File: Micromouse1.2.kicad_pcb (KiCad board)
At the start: 2 copper layers, 70.4 x 87.9 mm, 117 parts, among them J1 USB_B, P1 CONN_01X4, Q1 Q_NMOS_DGS, Q2 Q_NMOS_DGS, Q3 Q_NMOS_DGS, Q4 Q_NMOS_DGS, Q5 Q_NMOS_DGS, Q6 Q_NMOS_DGS, U1 BAT54C, U10 CONN_02X03, U14 ferrite, U15 LMZ21701, U16 JST_Connector, U17 Switch_micromouse, U18 LMZ21701, U19 splitter, U2 DRV8833, U20 TPD3S014, U21 MKL02Z32VFG4, U22 LP38691, U23 MK66FX1M0, U24 Test_Point, U25 Test_Point, U26 Test_Point, U27 Test_Point, U28 Test_Point, U29 Test_Point, U3 ferrite, U30 Test_Point, U31 MPU-6500, U32 Motor_mount, U5 ferrite, U6 BAT54C, U9 CONN_02X03, Y1 Crystal_16MHz, Y2 32.768MHz

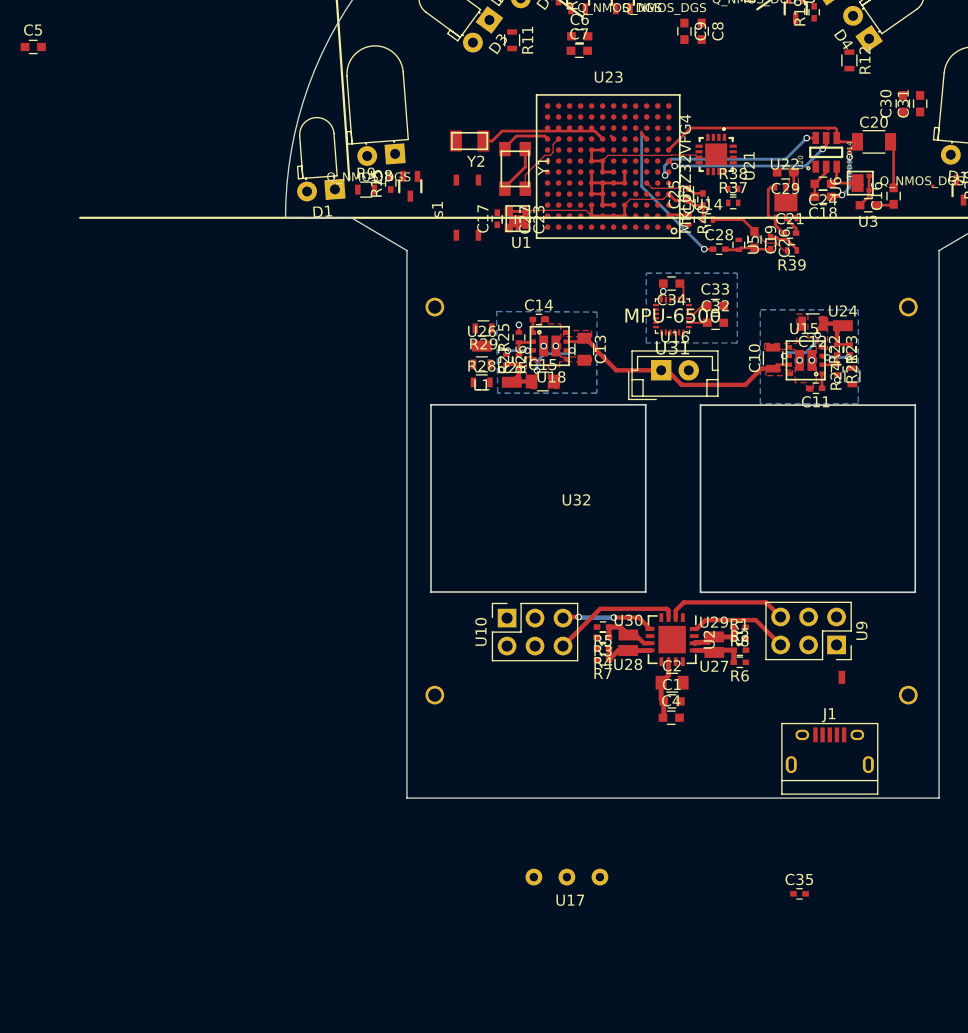
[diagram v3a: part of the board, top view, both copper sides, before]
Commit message: changed the MCU to MK20DX256VLH7
-changed the MCU to MK20DX256VLH7
-This branch is deprciated as I am changing back to the K66 series MCU
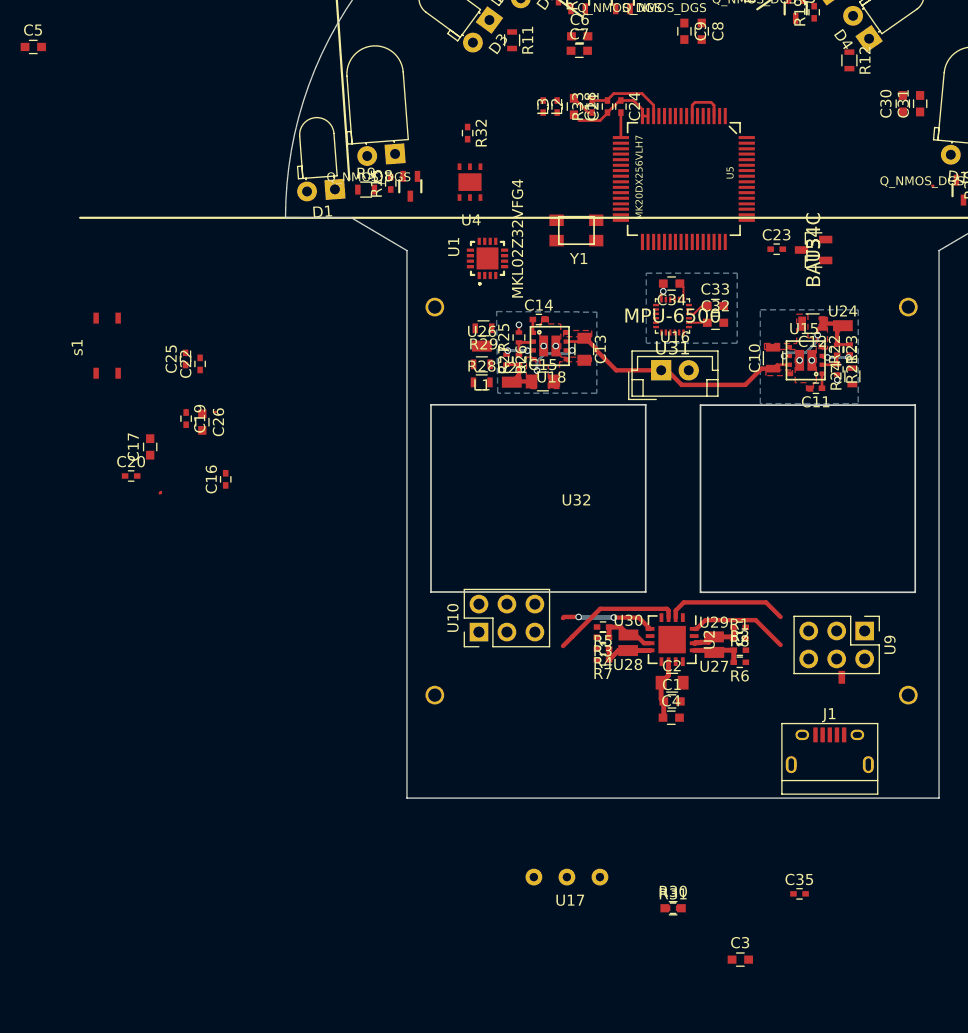
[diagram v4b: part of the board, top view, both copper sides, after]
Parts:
- removed C27, C29: 2.2uF, micromouse:C_0603
- removed C28: 0.1uF, micromouse:C_0402
- removed R37, R38: 33, Resistors_SMD:R_0402
- removed R39: 470, micromouse:R_0402
- removed R40: 100k, micromouse:R_0402
- removed U14: ferrite, micromouse:R_0402
- removed U20: TPD3S014, micromouse:TPD3S014
- removed U21: MKL02Z32VFG4, micromouse:MKL02Z32VFG4
- removed U22: LP38691, micromouse:LP38691
- removed U23: MK66FX1M0, micromouse:Microcontroller
- removed U6: BAT54C, micromouse:PMEG4010_DIODE
- removed Y2: 32.768MHz, micromouse:32.768_CRYSTAL
- added C3: 0.01uF, Capacitors_SMD:C_0603, F.Cu at (124.9, 129.1)
- added L2: Ferrite_Bead_Small, micromouse:C_0402, F.Cu at (107.0, 51.7)
- added L3: Ferrite_Bead_Small, micromouse:C_0402, F.Cu at (108.2, 51.7)
- added R30: R, micromouse:C_0603, F.Cu at (118.8, 124.5)
- added R31: 33, micromouse:C_0402, F.Cu at (118.8, 124.5)
- added R32: 33, micromouse:C_0402, F.Cu at (100.1, 54.1)
- added R33: 470, micromouse:C_0402, F.Cu at (111.4, 51.7)
- added U4: LP38691, micromouse:LP38691, F.Cu at (100.4, 58.5)
- C16: footprint micromouse:C_0603 -> Capacitors_SMD:C_0402
- C17, C26: value 0.1uF -> 2.2uF; footprint micromouse:C_0402 -> micromouse:C_0603
- C19, C24: value 2.2uF -> 0.1uF; footprint micromouse:C_0603 -> Capacitors_SMD:C_0402
- C20: value 100uF -> 0.1uF; footprint micromouse:C_1206 -> Capacitors_SMD:C_0402
- C21, C22: footprint micromouse:C_0402 -> Capacitors_SMD:C_0402
- C23: value 10nF -> 0.1uF; footprint micromouse:C_0402 -> Capacitors_SMD:C_0402
- C25: value 10nF -> 2.2uF; footprint micromouse:C_0402 -> Capacitors_SMD:C_0402
- J1: value USB_B -> USB_OTG
- U1: value BAT54C -> MKL02Z32VFG4; footprint micromouse:PMEG4010_DIODE -> micromouse:MKL02Z32VFG4
- U10, U9: footprint micromouse:Motors_connectors -> micromouse:Motor_Connector
- U3: value ferrite -> BAT54C; footprint micromouse:C_0603 -> PJC-Sandbox:SOT23-3P95_240X120L20X48N
- U5: value ferrite -> MK20DX256VLH7; footprint micromouse:R_0402 -> micromouse:LQFP-64
- Y1: value Crystal_16MHz -> Crystal_GND2
- moved C20 74.0 mm to (69.5, 85.2)
- moved C16 65.9 mm to (78.1, 85.5)
- moved C19 54.1 mm to (74.5, 80.0)
- moved C26 54.1 mm to (76.0, 80.3)
- moved C22 48.0 mm to (75.8, 75.0)
- moved C25 48.0 mm to (74.5, 74.6)
- moved C17 37.7 mm to (71.3, 82.6)
- moved s1 35.0 mm to (67.4, 73.4)
- moved C18 24.1 mm to (109.8, 51.7), turned to 270 degrees
- moved C23 23.0 mm to (128.2, 64.6), turned to 0 degrees
- moved C21 20.2 mm to (112.8, 51.7), turned to 90 degrees
- moved C24 19.6 mm to (114.0, 51.7), turned to 270 degrees
- moved Y1 7.89 mm to (110.0, 62.9), turned to 0 degrees
- moved U5 7.79 mm to (119.7, 58.2)
- moved U3 6.42 mm to (131.5, 64.7), turned to 90 degrees
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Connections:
- C17 pad 1: Net-(C17-Pad1) -> V_BAT
- C18 pad 2: GNDD -> Net-(C18-Pad2)
- C19 pad 2: Net-(C19-Pad2) -> GNDD
- C20 pad 1: Net-(C18-Pad1) -> Net-(C19-Pad1)
- C21 pad 1: Net-(C21-Pad1) -> Net-(C18-Pad2)
- C21 pad 2: GNDD -> Net-(C21-Pad2)
- C22 pad 1: Net-(C22-Pad1) -> Net-(C19-Pad1)
- C23 pad 1: Net-(C22-Pad1) -> Net-(C23-Pad1)
- C24 pad 1: Net-(C21-Pad1) -> Net-(C18-Pad2)
- C24 pad 2: GNDD -> Net-(C24-Pad2)
- C25 pad 1: Net-(C22-Pad1) -> Net-(C19-Pad1)
- C26 pad 1: Net-(C26-Pad1) -> Net-(C19-Pad1)
- C26 pad 2: Net-(C19-Pad2) -> GNDD
- J1 pad 1: Net-(J1-Pad1) -> Net-(C16-Pad1)
- J1 pad 5: Net-(J1-Pad5) -> GNDD
- J1 pad 6: (no net) -> GNDD
- U1 pad 1: Net-(C22-Pad1) -> Net-(C19-Pad1)
- U1 pad 2: Net-(U1-Pad2) -> GNDD
- U1 pad 3: Net-(C17-Pad1) -> Net-(U1-Pad3)
- U3 pad 1: Net-(C16-Pad1) -> Net-(C19-Pad1)
- U3 pad 2: Net-(U3-Pad2) -> V_BAT
- U5 pad 1: GNDD -> Net-(U5-Pad1)
- U5 pad 2: Net-(C19-Pad2) -> Net-(U5-Pad2)
- Y1 pad 1: Net-(U23-PadM12) -> Net-(U5-Pad32)
- Y1 pad 3: Net-(U23-PadM11) -> Net-(U5-Pad33)
- s1 pad 1: Net-(U21-Pad10) -> Net-(U1-Pad10)
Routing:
- net Net-(C22-Pad1): track 34.6 -> 0.00 mm, vias 1 -> 0
- net GNDD: track 35.2 -> 2.73 mm
- net Net-(R37-Pad1): track 16.0 -> 0.00 mm
- net Net-(U20-Pad6): track 15.8 -> 0.00 mm, vias 2 -> 0
- net Net-(C28-Pad1): track 13.8 -> 0.00 mm, vias 1 -> 0
- net Net-(U23-PadM7): track 11.5 -> 0.00 mm
- net Net-(C21-Pad1): track 10.3 -> 0.00 mm
- net Net-(C18-Pad2): track 0.00 -> 8.67 mm
- net Net-(C21-Pad2): track 0.00 -> 7.30 mm
- net Net-(C18-Pad1): track 9.29 -> 2.19 mm, vias 2 -> 0
- net Net-(U23-PadB7): track 6.71 -> 0.00 mm
- net Net-(U23-PadJ11): track 4.82 -> 0.00 mm
- net Net-(U23-PadM12): track 4.54 -> 0.00 mm
- net Net-(C19-Pad2): track 4.27 -> 0.00 mm
- net Net-(C19-Pad1): track 7.91 -> 4.22 mm
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- removed copper zone on F.Cu, net Net-(C22-Pad1)
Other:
- net class thintrackes added: clearance 0.1, trace_width 0.153, via_dia 0.6, via_drill 0.4
